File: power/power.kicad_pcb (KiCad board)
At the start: 2 copper layers, 100 x 100 mm, 34 parts, among them K1 MASTER_LIVE, K2 PREHEAT, M3_MOUNT VAL**, P1 CONTROL, P2 MAINS_INLET, P3 LOAD_OUTLET, Q1 BC817-40, Q2 BC817-40, U1 VTX214, U2 ACS710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

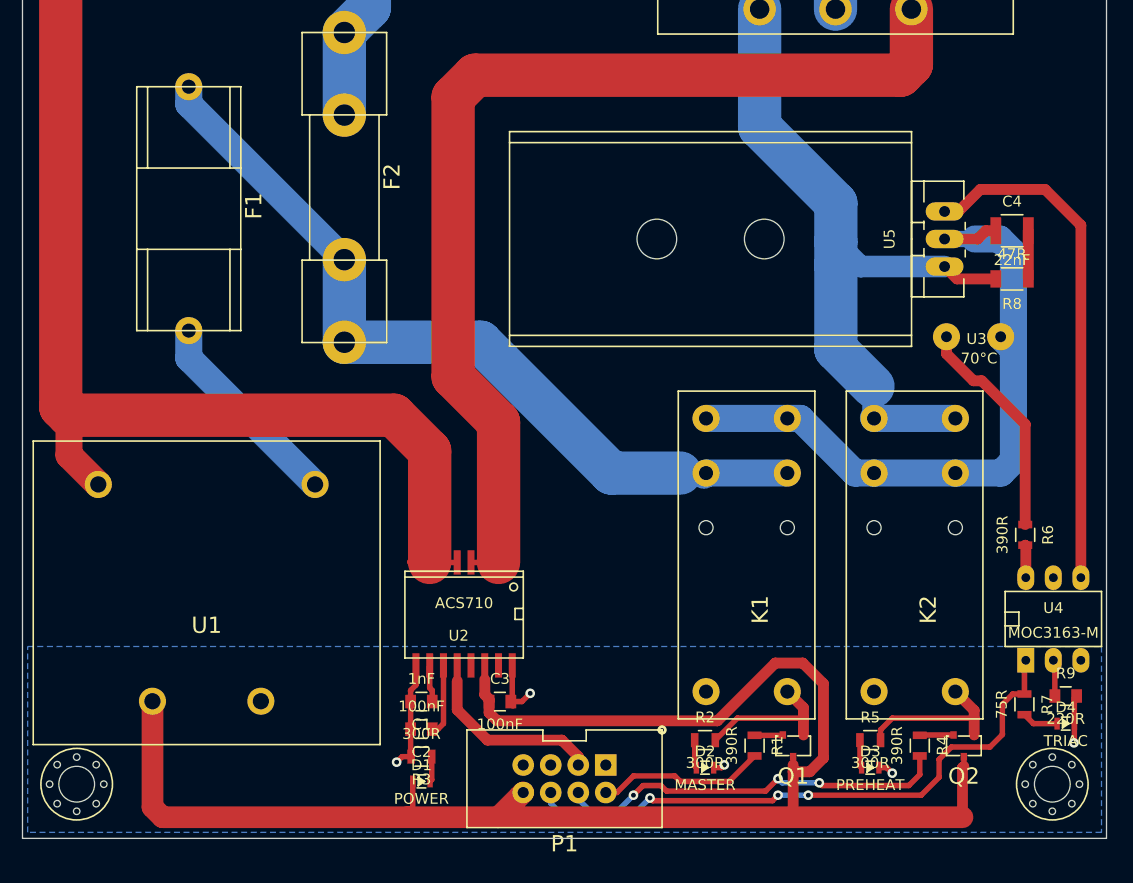
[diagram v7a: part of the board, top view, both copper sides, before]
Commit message: Added *correct* heatsink to schematic.
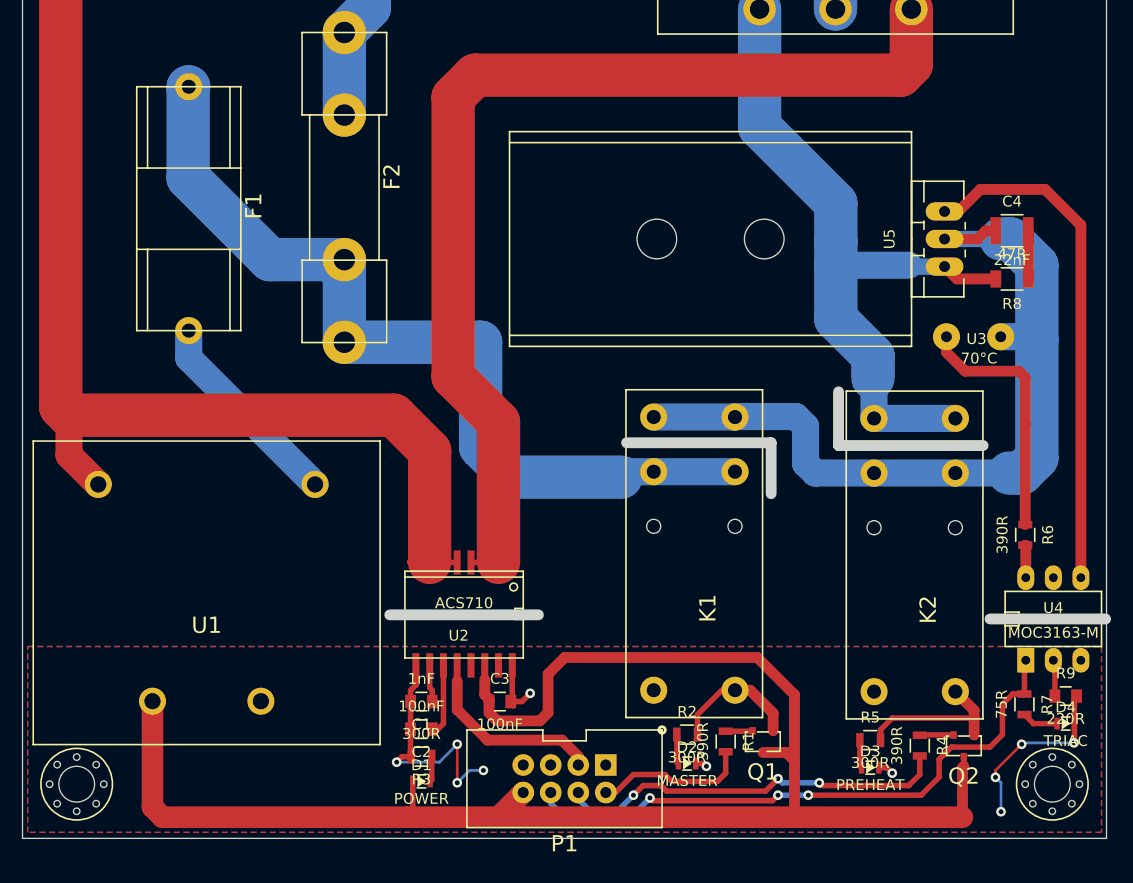
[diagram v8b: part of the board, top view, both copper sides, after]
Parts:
- moved K1 4.83 mm to (93.2, 110.8)
- moved Q1 2.82 mm to (98.3, 124.1)
- moved R1 2.69 mm to (94.9, 123.1)
- moved R2 1.73 mm to (91.3, 122.4)
- moved D2 1.69 mm to (91.3, 125.1)
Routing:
- net GND: track 23.4 -> 48.4 mm, vias 5 -> 11
- net TRIAC_MAINS: track 64.3 -> 76.4 mm
- net MAINS_LIVE: track 75.7 -> 80.6 mm
- net Net-(R6-Pad1): track 20.8 -> 23.2 mm
- net Net-(K1-Pad2): track 13.6 -> 12.3 mm
- net +5V: track 153.0 -> 151.7 mm
- net MASTER_RELAY: track 15.5 -> 14.3 mm
- net LOAD_LIVE: track 65.9 -> 65.1 mm
- added copper zone on F.Cu, net GND
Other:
- outline, holes or cut-outs redrawn
